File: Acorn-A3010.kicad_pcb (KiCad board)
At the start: 4 copper layers, 382 x 205 mm, 256 parts, among them IC11 HM514260AZ8, IC12 DS2401+, IC13 ARM250, IC14 4HCT574, IC15 4HCT574, IC16 MC1489, IC17 0296061, IC18 0296062, IC19 MC1488, IC2 80C51, IC20 74HC138, IC21 HM514260AJ8, IC22 HM514260AJ8, IC23 MC1489, IC24 82C711, IC25 74HC139, IC27 74AC32, IC3 74LS145, IC4 74LS145, IC5 PCF8583, IC6 HM514260AZ8, IC7 74LS366, IC8 74HCT14, IC9 74LS241, Q3 BC849, SW1 SW_Push_DPDT, U1 MC7905, X2 32.768KHz, X4 72.0MHz, X5 25.175MHz, X7 24MHz

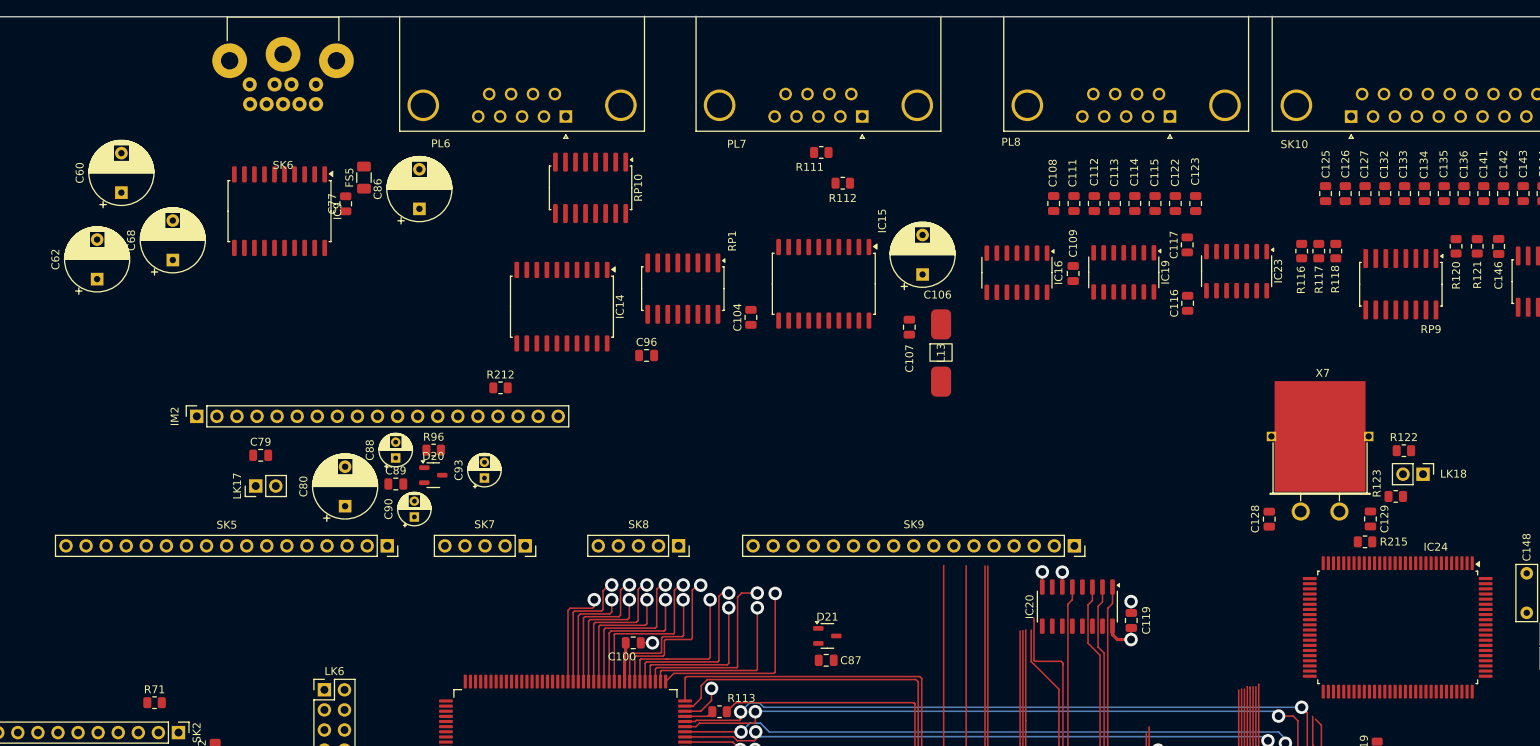
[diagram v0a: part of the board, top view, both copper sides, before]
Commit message: fix port reference locations and lock components
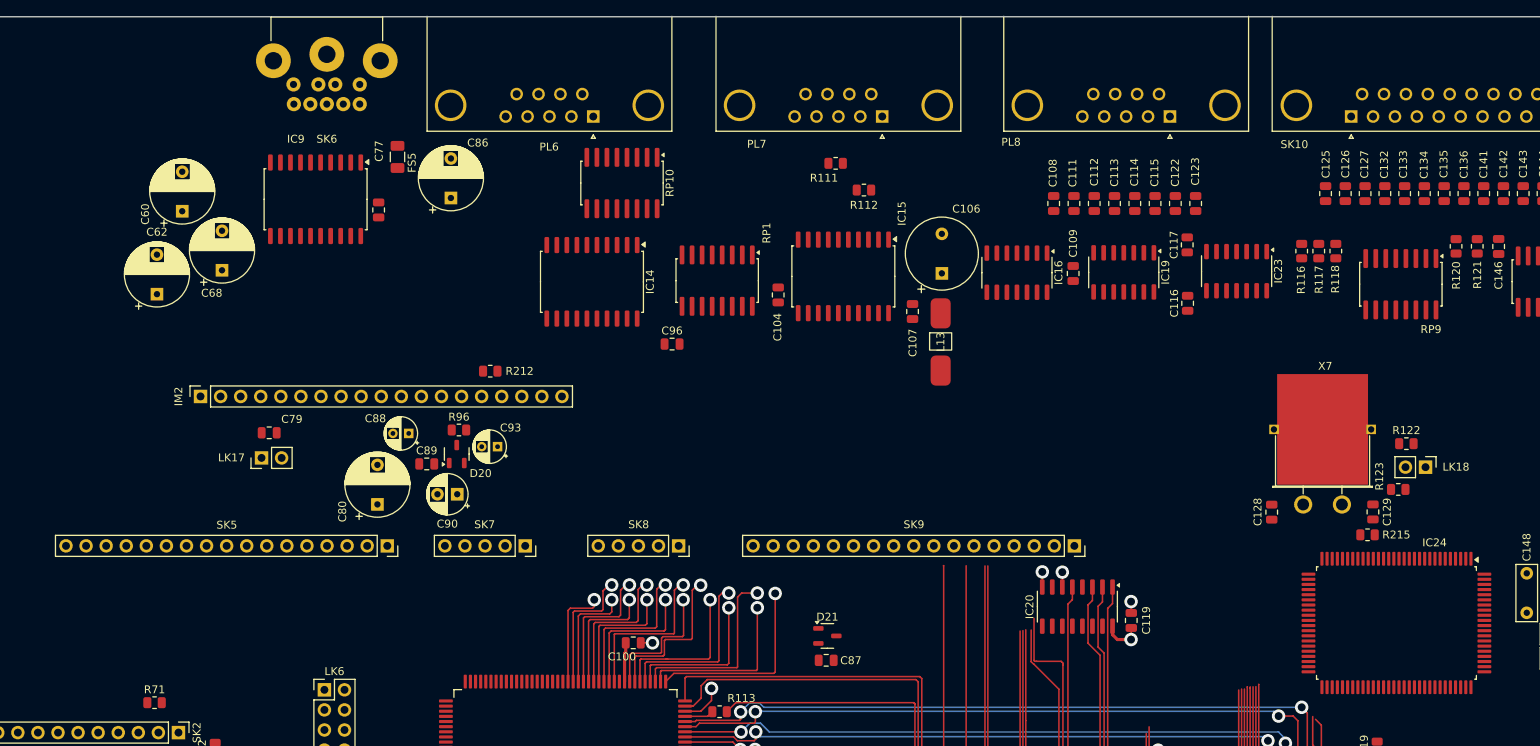
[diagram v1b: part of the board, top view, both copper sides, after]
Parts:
- C106: footprint Capacitor_THT:CP_Radial_D8.0mm_P5.00mm -> Capacitor_THT:CP_Radial_Tantal_D9.0mm_P5.00mm
- C90: footprint Capacitor_THT:CP_Radial_D4.0mm_P2.00mm -> Capacitor_THT:CP_Radial_D5.0mm_P2.50mm
- moved C60 8.05 mm to (178.6, 54.2)
- moved C62 7.81 mm to (175.4, 64.7)
- moved C68 6.36 mm to (183.6, 61.7)
- moved C90 6.13 mm to (213.4, 90.0), turned to 180 degrees
- moved SK6 5.54 mm to (196.9, 48.9)
- moved FS5 4.98 mm to (205.8, 47.4)
- moved IC14 4.93 mm to (230.4, 63.2)
- moved IC9 4.80 mm to (195.5, 52.7)
- moved C89 4.66 mm to (209.5, 86.2)
- moved C104 4.47 mm to (254.0, 64.8)
- moved RP1 4.46 mm to (246.3, 63.0)
- moved C93 4.30 mm to (218.5, 84.0), turned to 180 degrees
- moved C77 4.24 mm to (203.4, 54.1)
- moved C86 4.22 mm to (212.6, 52.6)
- moved C80 4.10 mm to (203.3, 91.3)
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
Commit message: fix perimter port positions
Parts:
- added C118: 220uF, Capacitor_THT:CP_Radial_D8.0mm_P5.00mm, F.Cu at (217.3, 67.3)
- added C124: 33nF, Capacitor_SMD:C_0805_2012Metric, F.Cu at (188.1, -9.63)
- added C225: 10nF, Capacitor_SMD:C_0805_2012Metric, F.Cu at (188.1, -6.62)
- added C226: 10nF, Capacitor_SMD:C_0805_2012Metric, F.Cu at (188.1, -3.61)
- added C69: 47nF, Capacitor_SMD:C_0805_2012Metric, F.Cu at (181.7, 67.5)
- added C78: 47uF, Capacitor_THT:CP_Radial_D8.0mm_P5.00mm, F.Cu at (204.5, 71.2)
- added Ge: LOGO, PowerBoard:BoardFolk, F.Cu at (49.3, 200.2)
- added H1: MountingHole, MountingHole:MountingHole_3.2mm_M3, F.Cu at (22.3, 33.2)
- added H2: MountingHole, MountingHole:MountingHole_3.2mm_M3, F.Cu at (22.3, 231.0)
- added H3: MountingHole, MountingHole:MountingHole_3.2mm_M3, F.Cu at (59.2, 233.0)
- added H4: MountingHole, MountingHole:MountingHole_3.2mm_M3, F.Cu at (240.1, 233.0)
- added H5: MountingHole, MountingHole:MountingHole_3.2mm_M3, F.Cu at (397.1, 33.2)
- added H6: MountingHole, MountingHole:MountingHole_3.2mm_M3, F.Cu at (397.1, 231.0)
- added H7: MountingHole, MountingHole:MountingHole_3.2mm_M3, F.Cu at (91.7, 37.1)
- added H8: MountingHole, MountingHole:MountingHole_3.2mm_M3, F.Cu at (91.7, 124.8)
- added IC10: LM386, Package_SO:SOIC-8_3.9x4.9mm_P1.27mm, F.Cu at (193.4, 70.7)
- added LK19: Internal Speaker, Connector_PinHeader_2.54mm:PinHeader_1x02_P2.54mm_Vertical, F.Cu at (374.4, 128.7)
- added LK30: Filter Ground, Connector_PinHeader_2.54mm:PinHeader_1x02_P2.54mm_Vertical, F.Cu at (167.0, 50.6)
- added R51: 3R3, Resistor_SMD:R_0805_2012Metric, F.Cu at (173.6, 43.8)
- added R65: 4K7, Resistor_SMD:R_0805_2012Metric, F.Cu at (178.7, 45.2)
- added R66: 4K7, Resistor_SMD:R_0805_2012Metric, F.Cu at (178.7, 47.6)
- added R68: 3R3, Resistor_SMD:R_0805_2012Metric, F.Cu at (182.8, 52.0)
- added R69: 10R, Resistor_SMD:R_0805_2012Metric, F.Cu at (181.8, 71.6)
- added R81: 4K7, Resistor_SMD:R_0805_2012Metric, F.Cu at (192.1, 61.0)
- added R82: 330R, Resistor_SMD:R_0805_2012Metric, F.Cu at (195.5, 61.0)
- added SK1: DE15_Receptacle_HighDensity_MountingHoles, Connector_Dsub:DSUB-15-HD_Female_Horizontal_P2.29x1.98mm_EdgePinOffset8.35mm_Housed_MountingHolesOffset10.89mm, F.Cu at (148.8, 42.3)
- added SK4: Stereo Headphones, Acorn:Jack_3.5mm_CUI_SJ1-3525N_Horizontal, F.Cu at (178.4, 33.0)
- C88: footprint Capacitor_THT:CP_Radial_D4.0mm_P2.00mm -> Capacitor_THT:CP_Radial_D5.0mm_P2.50mm
- moved LK13 36.0 mm to (28.7, 152.6), turned to -90 degrees
- moved C14 12.1 mm to (90.6, 143.9)
- moved C16 12.1 mm to (90.6, 153.5)
- moved R79 6.43 mm to (168.4, 220.8)
- moved C76 6.43 mm to (178.3, 206.8)
- moved IC7 6.43 mm to (172.9, 213.6)
- moved R64 6.43 mm to (176.1, 205.6)
- moved R77 6.43 mm to (171.9, 205.6)
- moved R78 6.43 mm to (174.0, 205.6)
- moved R80 6.43 mm to (179.7, 220.2)
- moved C60 6.26 mm to (173.0, 57.1)
- moved C62 6.26 mm to (169.8, 67.6)
- moved C68 6.26 mm to (178.1, 64.6)
- moved R72 5.24 mm to (186.9, 125.7)
- moved SK3 5.07 mm to (134.4, 126.5)
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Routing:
- net /CPU/La2: track 160.4 -> 196.5 mm
- net /CPU/La4: track 90.9 -> 122.1 mm, vias 1 -> 2
- net /CPU/La6: track 85.2 -> 110.8 mm
- net GND: track 61.8 -> 85.0 mm
- net /CPU/La3: track 156.2 -> 177.7 mm, vias 0 -> 2
- net /CPU/La5: track 86.2 -> 106.5 mm, vias 1 -> 2
- net Net-(IC24-Drvtyp): track 0.00 -> 17.7 mm
- net Net-(IC24-Pren): track 0.00 -> 15.4 mm
- net /CPU/La7: track 132.0 -> 147.3 mm, vias 1 -> 3
- net /CPU/La8: track 123.5 -> 138.5 mm, vias 1 -> 3
- net Net-(C128-Pad1): track 0.00 -> 13.6 mm
- net Net-(IC24-Oscl/Clk): track 0.00 -> 10.5 mm
- net /CPU/La9: track 110.4 -> 120.3 mm, vias 1 -> 3
- net /IO/~{Readdata}: track 9.34 -> 15.9 mm, vias 0 -> 1
- net /CPU/Bd0: track 6.45 -> 11.8 mm, vias 0 -> 1
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- added copper zone on B.Cu, net GND
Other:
- outline, holes or cut-outs redrawn
- board text added: "MAIN PCB 0194,003 ISS.1"
- board text added: "The Board Folk Team 2024"
